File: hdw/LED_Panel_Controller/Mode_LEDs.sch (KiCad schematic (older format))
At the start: 40 parts, among them U2301 74LVC1G97, U2302 74LVC1G97, U2303 74LVC1G97, U2304 74LVC1G97, U2305 74LVC1G97, U2306 74LVC1G97, U2307 74LVC1G97, U2308 74LVC1G97

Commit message: having a mid-project crisis
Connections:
- net WIFI_Stream_Mode_LED renamed MLVDS_Stream_Mode_LED
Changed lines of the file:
@@
 $EndComp
 Text GLabel 1560 3460 0    50   Input ~ 0
-WIFI_Stream_Mode_LED
+MLVDS_Stream_Mode_LED
 $Comp
 L Custom_Library:C_Custom C?

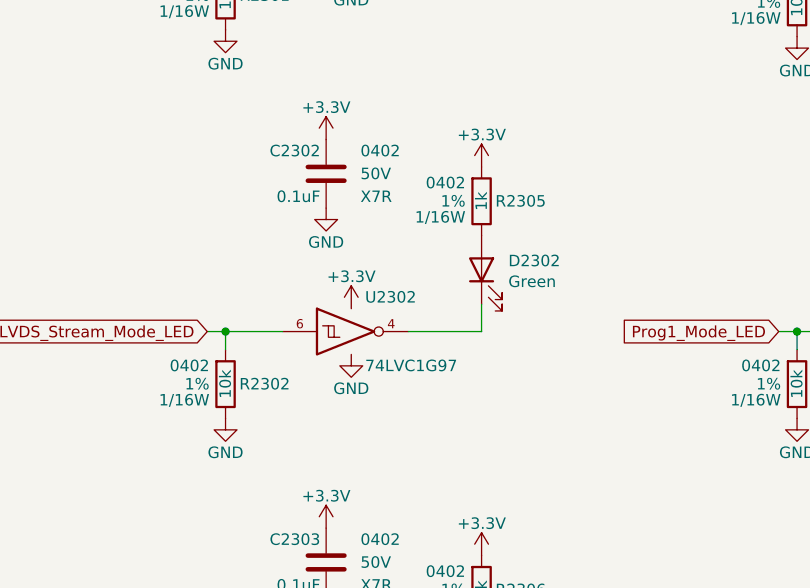
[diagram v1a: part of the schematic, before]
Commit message: reworked schematic to use MLVDS connector instead of wifi module
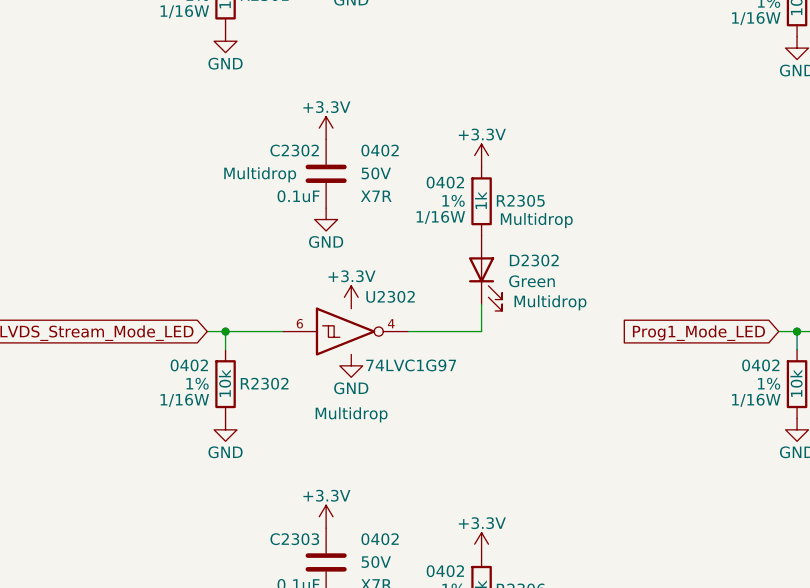
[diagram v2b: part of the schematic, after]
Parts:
- C2302, D2302, R2305, U2302: Configuration (none) -> Multidrop
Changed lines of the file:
@@
 Sheet 23 34
 Title "LED Panel Controller"
-Date "2021-03-31"
+Date "2021-05-30"
 Rev "A"
 Comp "Drew Maatman"
@@
 F 6 "50V" H 1930 2770 50  0000 R CNN "Voltage"
 F 7 "X7R" H 1930 2670 50  0000 R CNN "Dielectric"
+F 8 "Multidrop" H 2370 2770 50  0000 C CNN "Configuration"
 	1    2080 2770
 	-1   0    0    -1
@@
 F 3 "~" H 2760 3190 50  0001 C CNN
 F 4 "1497-1219-1-ND" H -2400 -3130 50  0001 C CNN "Digi-Key PN"
+F 5 "Multidrop" V 2620 2890 50  0000 C CNN "Configuration"
 	1    2760 3190
 	0    -1   -1   0
@@
 F 6 "1/16W" H 2830 2820 50  0000 L CNN "Wattage"
 F 7 "RMCF0402FT1K00CT-ND" H 3060 3290 60  0001 C CNN "Digi-Key PN"
+F 8 "Multidrop" H 2520 2810 50  0000 C CNN "Configuration"
 	1    2760 2890
 	-1   0    0    -1
@@
 F 3 "http://www.ti.com/lit/ds/symlink/sn74lvc1g97.pdf" H 2240 3460 50  0001 C CNN
 F 4 "1727-1772-1-ND" H 2190 3460 50  0001 C CNN "Digi-Key PN"
+F 5 "Multidrop" H 2190 3100 50  0000 C CNN "Configuration"
 	1    2190 3460
 	1    0    0    -1

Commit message: added BOMs, some consolidation
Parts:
- C2301, C2302, C2303, C2304, C2305, C2306, C2307, C2308: Digi-Key PN 490-10701-1-ND -> 490-10698-1-ND
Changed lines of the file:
@@
 F 2 "Capacitors_SMD:C_0402" H 2118 920 50  0001 C CNN
 F 3 "" H 2105 1170 50  0001 C CNN
-F 4 "490-10701-1-ND" H 2505 1570 60  0001 C CNN "Digi-Key PN"
+F 4 "490-10698-1-ND" H 2505 1570 60  0001 C CNN "Digi-Key PN"
 F 5 "0402" H 1930 1170 50  0000 R CNN "display_footprint"
 F 6 "50V" H 1930 1070 50  0000 R CNN "Voltage"
@@
 F 2 "Capacitors_SMD:C_0402" H 4618 950 50  0001 C CNN
 F 3 "" H 4605 1200 50  0001 C CNN
-F 4 "490-10701-1-ND" H 5005 1600 60  0001 C CNN "Digi-Key PN"
+F 4 "490-10698-1-ND" H 5005 1600 60  0001 C CNN "Digi-Key PN"
 F 5 "0402" H 4430 1200 50  0000 R CNN "display_footprint"
 F 6 "50V" H 4430 1100 50  0000 R CNN "Voltage"
@@
 F 2 "Capacitors_SMD:C_0402" H 2118 2620 50  0001 C CNN
 F 3 "" H 2105 2870 50  0001 C CNN
-F 4 "490-10701-1-ND" H 2505 3270 60  0001 C CNN "Digi-Key PN"
+F 4 "490-10698-1-ND" H 2505 3270 60  0001 C CNN "Digi-Key PN"
 F 5 "0402" H 1930 2870 50  0000 R CNN "display_footprint"
 F 6 "50V" H 1930 2770 50  0000 R CNN "Voltage"
@@
 F 2 "Capacitors_SMD:C_0402" H 4618 2620 50  0001 C CNN
 F 3 "" H 4605 2870 50  0001 C CNN
-F 4 "490-10701-1-ND" H 5005 3270 60  0001 C CNN "Digi-Key PN"
+F 4 "490-10698-1-ND" H 5005 3270 60  0001 C CNN "Digi-Key PN"
 F 5 "0402" H 4430 2870 50  0000 R CNN "display_footprint"
 F 6 "50V" H 4430 2770 50  0000 R CNN "Voltage"
@@
 F 2 "Capacitors_SMD:C_0402" H 7118 2620 50  0001 C CNN
 F 3 "" H 7105 2870 50  0001 C CNN
-F 4 "490-10701-1-ND" H 7505 3270 60  0001 C CNN "Digi-Key PN"
+F 4 "490-10698-1-ND" H 7505 3270 60  0001 C CNN "Digi-Key PN"
 F 5 "0402" H 6930 2870 50  0000 R CNN "display_footprint"
 F 6 "50V" H 6930 2770 50  0000 R CNN "Voltage"
@@
 F 2 "Capacitors_SMD:C_0402" H 2118 4320 50  0001 C CNN
 F 3 "" H 2105 4570 50  0001 C CNN
-F 4 "490-10701-1-ND" H 2505 4970 60  0001 C CNN "Digi-Key PN"
+F 4 "490-10698-1-ND" H 2505 4970 60  0001 C CNN "Digi-Key PN"
 F 5 "0402" H 1930 4570 50  0000 R CNN "display_footprint"
 F 6 "50V" H 1930 4470 50  0000 R CNN "Voltage"
@@
 F 2 "Capacitors_SMD:C_0402" H 4618 4320 50  0001 C CNN
 F 3 "" H 4605 4570 50  0001 C CNN
-F 4 "490-10701-1-ND" H 5005 4970 60  0001 C CNN "Digi-Key PN"
+F 4 "490-10698-1-ND" H 5005 4970 60  0001 C CNN "Digi-Key PN"
 F 5 "0402" H 4430 4570 50  0000 R CNN "display_footprint"
 F 6 "50V" H 4430 4470 50  0000 R CNN "Voltage"
@@
 F 2 "Capacitors_SMD:C_0402" H 7118 950 50  0001 C CNN
 F 3 "" H 7105 1200 50  0001 C CNN
-F 4 "490-10701-1-ND" H 7505 1600 60  0001 C CNN "Digi-Key PN"
+F 4 "490-10698-1-ND" H 7505 1600 60  0001 C CNN "Digi-Key PN"
 F 5 "0402" H 6930 1200 50  0000 R CNN "display_footprint"
 F 6 "50V" H 6930 1100 50  0000 R CNN "Voltage"
